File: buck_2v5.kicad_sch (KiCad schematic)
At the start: 20 parts, among them U3 TPS564257DRLR

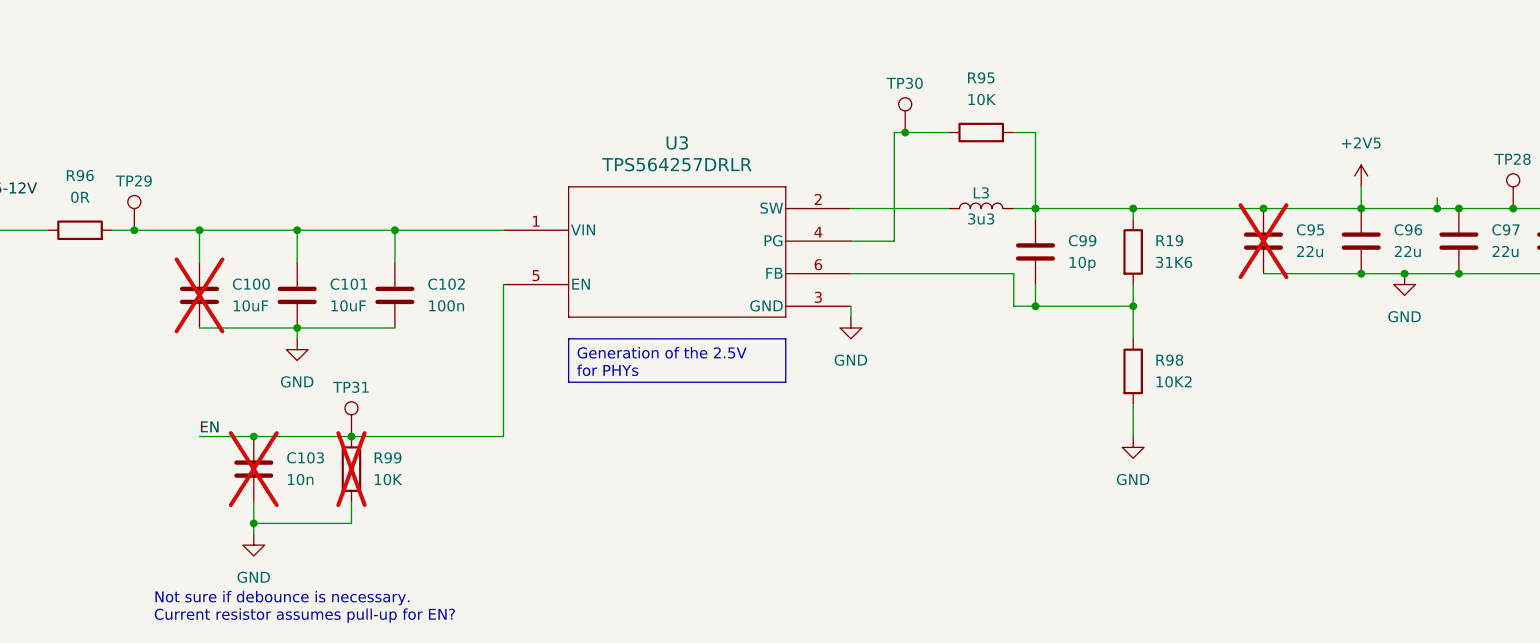
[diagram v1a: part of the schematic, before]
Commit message: updates resistors and inductor symbol in 2V5 converter
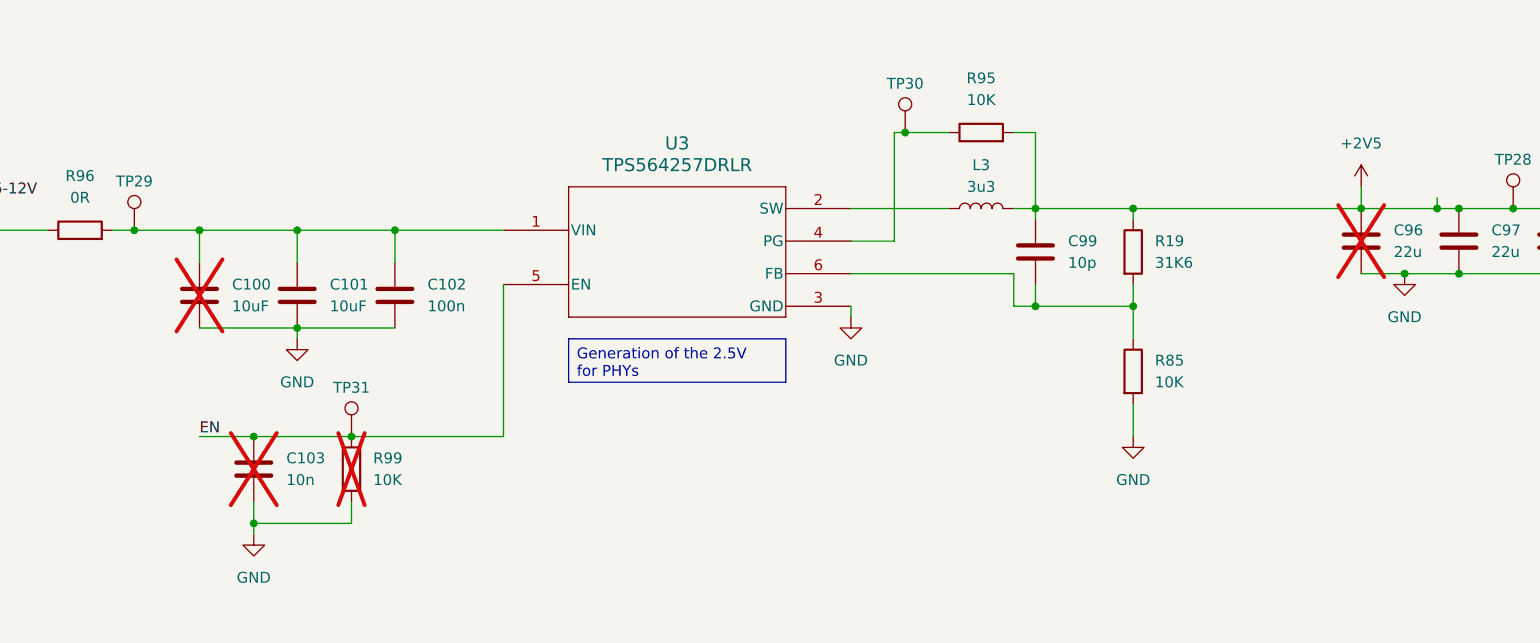
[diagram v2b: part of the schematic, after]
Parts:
- removed C95: 22u, KL:C_0603, symbol KL_C:C_22u_10V_X5R_0603_20
- removed R98: 10K2, KL_Footprints:C_0603, symbol KL_R:R_10K2_100mW_1_0603
- added R85: 10K, KL_Footprints:C_0603, symbol KL_R:R_10K_100mW_1_0603
- C100, C103, R99: now left out of the parts list
- C96: now not fitted; now left out of the parts list
- L3: symbol KL_L:L_3u3_8A -> KL_L:L_3u3_8A_20pct_7LX7W; I_max_in_A (none) -> 8; Max Current 8 -> (none); Package_in_mm (none) -> L7XW7; Tolerance_in_pct (none) -> 20
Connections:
- net GND: now also R85.2
- net at C99.2, R19.2, U3.6 (FB): now also R85.1
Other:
- note removed: "Not sure if debounce is necessary. Current resistor assumes pull-up for EN?"

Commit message: fixes ERC errors in DC/DC converters
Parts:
- C100: footprint Capacitor_SMD:C_0201_0603Metric -> KL_Footprints:C_0603; now in the parts list
- C101, C102, C98, C99: footprint Capacitor_SMD:C_0201_0603Metric -> KL_Footprints:C_0603
- C96: footprint KL:C_0603 -> KL_Footprints:C_0603; now in the parts list
- C97: footprint KL:C_0603 -> KL_Footprints:C_0603
- L3: footprint KL:L_3u3_EXLA1V0603 -> KL_Footprints:EXLA1V0603
- R19, R85, R95: footprint KL_Footprints:C_0603 -> KL_Footprints:R_0603
- R99: footprint KL_Footprints:C_0603 -> KL_Footprints:R_0603; now in the parts list
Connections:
- net +2V5 renamed +2V5_OUT
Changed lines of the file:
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@@
 	)
 	(junction
+		(at 93.98 81.28)
+		(diameter 0)
+		(color 0 0 0 0)
+	)
+	(junction
 		(at 229.87 78.74)
 		(diameter 0)
@@
 	(wire
 		(pts
-			(xy 40.64 38.1) (xy 48.26 38.1)
+			(xy 40.64 38.1) (xy 52.07 38.1)
 		)
 		(stroke
@@
 	(wire
 		(pts
-			(xy 212.09 76.2) (xy 212.09 78.74)
-		)
-		(stroke
-			(width 0)
-			(type default)
-		)
-	)
-	(wire
-		(pts
 			(xy 220.98 77.47) (xy 220.98 78.74)
 		)
@@
 	(wire
 		(pts
+			(xy 93.98 81.28) (xy 87.63 81.28)
+		)
+		(stroke
+			(width 0)
+			(type default)
+		)
+	)
+	(wire
+		(pts
 			(xy 171.45 69.85) (xy 173.99 69.85)
 		)
@@
 	(wire
 		(pts
-			(xy 40.64 41.91) (xy 48.26 41.91)
+			(xy 40.64 41.91) (xy 52.07 41.91)
 		)
 		(stroke
@@
 	(wire
 		(pts
-			(xy 40.64 45.72) (xy 48.26 45.72)
+			(xy 40.64 45.72) (xy 52.07 45.72)
 		)
 		(stroke
@@
 	(wire
 		(pts
-			(xy 99.06 81.28) (xy 87.63 81.28)
+			(xy 99.06 81.28) (xy 93.98 81.28)
 		)
 		(stroke
@@
 	)
 	(label "5-12V"
-		(at 48.26 41.91 180)
+		(at 52.07 41.91 180)
 		(effects
 			(font
@@
 	)
 	(label "EN"
-		(at 48.26 45.72 180)
+		(at 52.07 45.72 180)
 		(effects
 			(font
@@
 		)
 	)
-	(hierarchical_label "2V5"
+	(label "+2V5_OUT"
+		(at 193.04 78.74 0)
+		(effects
+			(font
+				(size 1.27 1.27)
+			)
+			(justify left bottom)
+		)
+	)
+	(label "+2V5_OUT"
+		(at 52.07 38.1 180)
+		(effects
+			(font
+				(size 1.27 1.27)
+			)
+			(justify right bottom)
+		)
+	)
+	(hierarchical_label "+2V5_OUT"
 		(shape output)
 		(at 40.64 38.1 180)
@@
 	)
 	(symbol
+		(lib_id "KL_Flags:PWR_FLAG")
+		(at 93.98 81.28 0)
+		(unit 1)
+		(exclude_from_sim no)
+		(in_bom yes)
+		(on_board yes)
+		(dnp no)
+		(fields_autoplaced yes)
+		(property "Reference" "#FLG05"
+			(at 93.98 79.375 0)
+			(effects
+				(font
+					(size 1.27 1.27)
+				)
+				(hide yes)
+			)
+		)
+		(property "Value" "PWR_FLAG"
+			(at 93.98 76.2 0)
+			(effects
+				(font
+					(size 1.27 1.27)
+				)
+			)
+		)
+		(property "Footprint" ""
+			(at 93.98 81.28 0)
+			(effects
+				(font
+					(size 1.27 1.27)
+				)
+				(hide yes)
+			)
+		)
+		(property "Datasheet" "~"
+			(at 93.98 81.28 0)
+			(effects
+				(font
+					(size 1.27 1.27)
+				)
+				(hide yes)
+			)
+		)
+		(property "Description" "Special symbol for telling ERC where power comes from"
+			(at 93.98 81.28 0)
+			(effects
+				(font
+					(size 1.27 1.27)
+				)
+				(hide yes)
+			)
+		)
+		(pin "1"
+		)
+		(instances
+			(project ""
+				(path "/d4536448-b109-4159-96e2-3dc21baf2d6e/0b7d9af9-83c1-43fa-a7a0-a33d0a00ea9c/c6e71b93-7134-487d-a04c-584c6081214b"
+					(reference "#FLG05")
+					(unit 1)
+				)
+			)
+		)
+	)
+	(symbol
 		(lib_id "KL_TP:TestPoint")
 		(at 229.87 78.74 0)
@@
 			)
 		)
-		(property "Footprint" "Capacitor_SMD:C_0201_0603Metric"
+		(property "Footprint" "KL_Footprints:C_0603"
 			(at 100.0252 92.71 0)
 			(effects
@@
 			)
 		)
-		(property "Footprint" "Capacitor_SMD:C_0201_0603Metric"
+		(property "Footprint" "KL_Footprints:C_0603"
 			(at 235.9152 86.36 0)
 			(effects
@@
 		(unit 1)
 		(exclude_from_sim no)
-		(in_bom no)
+		(in_bom yes)
 		(on_board yes)
 		(dnp yes)
@@
 			)
 		)
-		(property "Footprint" "KL:C_0603"
+		(property "Footprint" "KL_Footprints:C_0603"
 			(at 213.0552 86.36 0)
 			(effects
@@
 			)
 		)
-		(property "Footprint" "KL_Footprints:C_0603"
+		(property "Footprint" "KL_Footprints:R_0603"
 			(at 183.642 97.79 90)
 			(effects
@@
 		(unit 1)
 		(exclude_from_sim no)
-		(in_bom no)
+		(in_bom yes)
 		(on_board yes)
 		(dnp yes)
@@
 			)
 		)
-		(property "Footprint" "Capacitor_SMD:C_0201_0603Metric"
+		(property "Footprint" "KL_Footprints:C_0603"
 			(at 77.1652 92.71 0)
 			(effects
@@
 			)
 		)
-		(property "Footprint" "KL_Footprints:C_0603"
+		(property "Footprint" "KL_Footprints:R_0603"
 			(at 183.642 83.82 90)
 			(effects
@@
 			)
 		)
-		(property "Footprint" "KL_Footprints:C_0603"
+		(property "Footprint" "KL_Footprints:R_0603"
 			(at 167.64 71.628 90)
 			(effects
@@
 			)
 		)
-		(property "Footprint" "KL:C_0603"
+		(property "Footprint" "KL_Footprints:C_0603"
 			(at 224.4852 86.36 0)
 			(effects
@@
 			)
 		)
-		(property "Footprint" "KL:L_3u3_EXLA1V0603"
+		(property "Footprint" "KL_Footprints:EXLA1V0603"
 			(at 163.83 71.12 0)
 			(effects
@@
 		(unit 1)
 		(exclude_from_sim no)
-		(in_bom no)
+		(in_bom yes)
 		(on_board yes)
 		(dnp yes)
@@
 			)
 		)
-		(property "Footprint" "KL_Footprints:C_0603"
+		(property "Footprint" "KL_Footprints:R_0603"
 			(at 92.202 109.22 90)
 			(effects
@@
 			)
 		)
-		(property "Footprint" "Capacitor_SMD:C_0201_0603Metric"
+		(property "Footprint" "KL_Footprints:C_0603"
 			(at 174.9552 87.63 0)
 			(effects
@@
 			)
 		)
-		(property "Footprint" "Capacitor_SMD:C_0201_0603Metric"
+		(property "Footprint" "KL_Footprints:C_0603"
 			(at 88.5952 92.71 0)
 			(effects
@@
 					(unit 1)
 				)
-			)
-		)
-	)
-	(symbol
-		(lib_id "KL_SYM_LOCAL:+2V5")
-		(at 212.09 76.2 0)
-		(unit 1)
-		(exclude_from_sim no)
-		(in_bom yes)
-		(on_board yes)
-		(dnp no)
-		(fields_autoplaced yes)
-		(property "Reference" "#PWR3"
-			(at 212.09 80.01 0)
-			(effects
-				(font
-					(size 1.27 1.27)
-				)
-				(hide yes)
-			)
-		)
-		(property "Value" "+2V5"
-			(at 212.09 71.12 0)
-			(effects
-				(font
-					(size 1.27 1.27)
-				)
-			)
-		)
-		(property "Footprint" ""
-			(at 212.09 76.2 0)
-			(effects
-				(font
-					(size 1.27 1.27)
-				)
-				(hide yes)
-			)
-		)
-		(property "Datasheet" ""
-			(at 212.09 76.2 0)
-			(effects
-				(font
-					(size 1.27 1.27)
-				)
-				(hide yes)
-			)
-		)
-		(property "Description" "Power symbol creates a global label with name \"+2V5\""
-			(at 212.09 76.2 0)
-			(effects
-				(font
-					(size 1.27 1.27)
-				)
-				(hide yes)
-			)
-		)
-		(pin "1"
-		)
-		(instances
-			(project "switch"
-				(path "/cd936d40-9035-4ec8-bcf8-38758f995fb0/c6e71b93-7134-487d-a04c-584c6081214b"
-					(reference "#PWR?")
-					(unit 1)
-				)
-			)
-			(project "shish-lan"
-				(path "/d4536448-b109-4159-96e2-3dc21baf2d6e/0b7d9af9-83c1-43fa-a7a0-a33d0a00ea9c/c6e71b93-7134-487d-a04c-584c6081214b"
-					(reference "#PWR3")
-					(unit 1)
-				)
-			)
-		)
-	)
-	(symbol
-		(lib_id "KL_SYM_LOCAL:+2V5")
-		(at 48.26 38.1 0)
-		(unit 1)
-		(exclude_from_sim no)
-		(in_bom yes)
-		(on_board yes)
-		(dnp no)
-		(fields_autoplaced yes)
-		(property "Reference" "#PWR9"
-			(at 48.26 41.91 0)
-			(effects
-				(font
-					(size 1.27 1.27)
-				)
-				(hide yes)
-			)
-		)
-		(property "Value" "+2V5"
-			(at 48.26 33.02 0)
-			(effects
-				(font
-					(size 1.27 1.27)
-				)
-			)
-		)
-		(property "Footprint" ""
-			(at 48.26 38.1 0)
-			(effects
-				(font
-					(size 1.27 1.27)
-				)
-				(hide yes)
-			)
-		)
-		(property "Datasheet" ""
-			(at 48.26 38.1 0)
-			(effects
-				(font
-					(size 1.27 1.27)
-				)
-				(hide yes)
-			)
-		)
-		(property "Description" "Power symbol creates a global label with name \"+2V5\""
-			(at 48.26 38.1 0)
-			(effects
-				(font
-					(size 1.27 1.27)
-				)
-				(hide yes)
-			)
-		)
-		(pin "1"
-		)
-		(instances
-			(project "switch"
-				(path "/cd936d40-9035-4ec8-bcf8-38758f995fb0/c6e71b93-7134-487d-a04c-584c6081214b"
-					(reference "#PWR?")
-					(unit 1)
-				)
-			)
-			(project ""
-				(path "/d4536448-b109-4159-96e2-3dc21baf2d6e/0b7d9af9-83c1-43fa-a7a0-a33d0a00ea9c/c6e71b93-7134-487d-a04c-584c6081214b"
-					(reference "#PWR9")
-					(unit 1)
-				)

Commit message: updates components from my library misconfiguration. Refs: #1
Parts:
- C103: footprint Capacitor_SMD:C_0201_0603Metric -> KL_Footprints:C_0603; now in the parts list
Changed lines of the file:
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@@
 		(unit 1)
 		(exclude_from_sim no)
-		(in_bom no)
+		(in_bom yes)
 		(on_board yes)
 		(dnp yes)
@@
 			)
 		)
-		(property "Footprint" "Capacitor_SMD:C_0201_0603Metric"
+		(property "Footprint" "KL_Footprints:C_0603"
 			(at 83.5152 113.03 0)
 			(effects

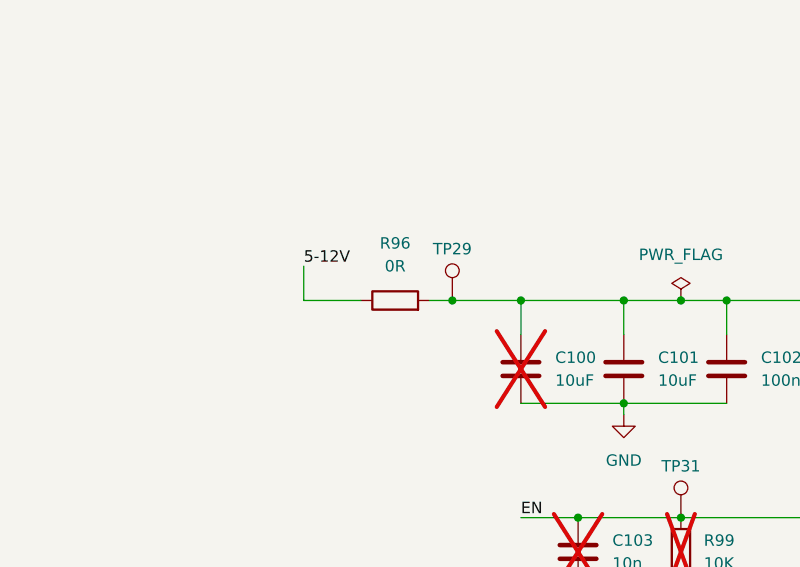
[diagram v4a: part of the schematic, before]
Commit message: removes unused busses, adds cheaper 0R resistor, clean up to fix ERC errors. Refs: #1
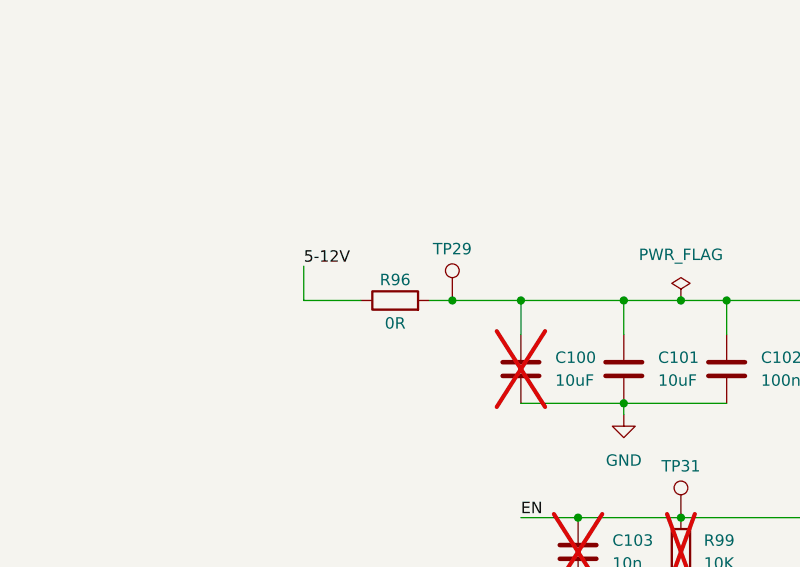
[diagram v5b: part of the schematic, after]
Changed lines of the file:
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@@
 		(on_board yes)
 		(dnp no)
-		(fields_autoplaced yes)
 		(property "Reference" "R96"
-			(at 62.23 74.93 90)
+			(at 62.23 78.994 90)
 			(effects
 				(font
@@
 		)
 		(property "Value" "0R"
-			(at 62.23 77.47 90)
+			(at 62.23 83.82 90)
 			(effects
 				(font
